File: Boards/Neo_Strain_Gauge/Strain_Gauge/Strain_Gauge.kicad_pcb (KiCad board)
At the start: 2 copper layers, 85 x 56 mm, 60 parts, among them J1 Screw_Terminal_01x03, J2 Screw_Terminal_01x03, J3 Screw_Terminal_01x03, J4 Screw_Terminal_01x03, J5 Conn_01x02, J6 USB_B_Micro, J7 Conn_02x10_Counter_Clockwise, J8 Conn_02x12_Counter_Clockwise, U1 W25Q128JVS, U2 NCP1117-3.3_SOT223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

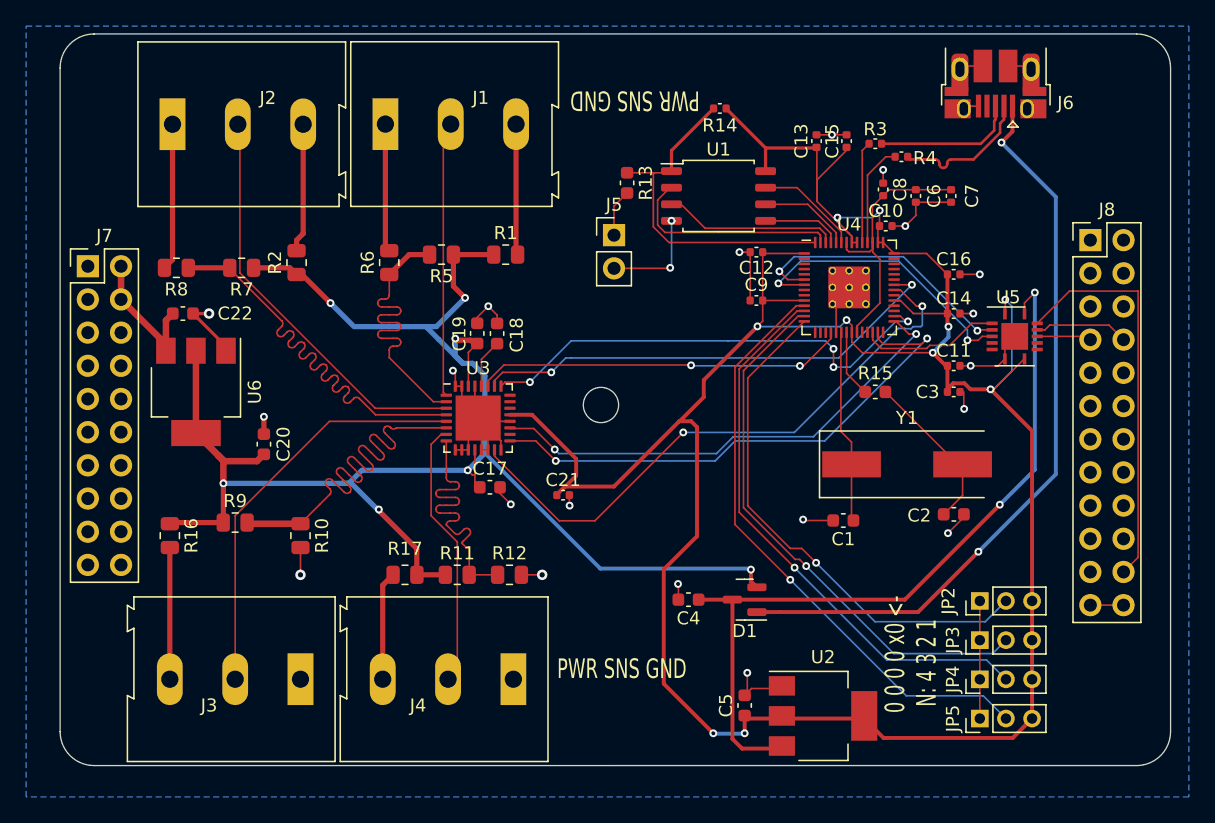
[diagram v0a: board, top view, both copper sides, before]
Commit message: Remove a LOT of signal noise on the oscillator
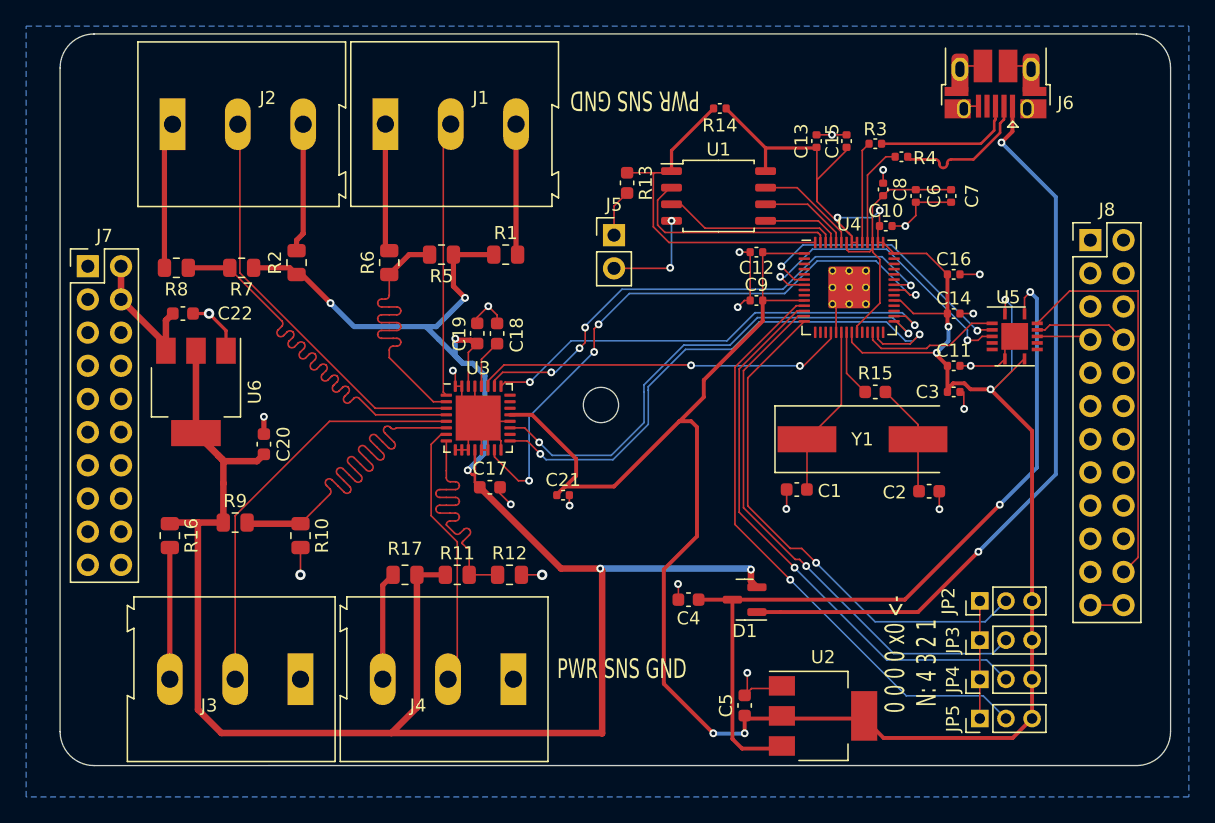
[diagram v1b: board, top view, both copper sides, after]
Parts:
- moved C1 4.28 mm to (157.0, 88.5)
- moved Y1 3.91 mm to (162.0, 84.6)
- moved C2 2.59 mm to (167.1, 88.6)
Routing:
- net +5V: track 132.9 -> 174.9 mm, vias 7 -> 6
- net +3V3: track 208.4 -> 200.2 mm, vias 10 -> 8
- net Net-(C2-Pad1): track 12.6 -> 8.66 mm
- net /GPIO24: track 36.8 -> 39.2 mm, vias 2 -> 4
- net /GPIO16: track 41.0 -> 43.0 mm
- net /XIN: track 14.8 -> 13.1 mm
- net /GPIO23: track 45.6 -> 47.3 mm, vias 2 -> 4
- net /GPIO18: track 37.8 -> 39.4 mm
- net GND: track 116.8 -> 116.1 mm, vias 22 -> 23
- net /GPIO19: track 36.7 -> 36.3 mm, vias 4 -> 2

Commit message: Anti-emi Aktion
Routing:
- net +5V: track 174.9 -> 226.2 mm, vias 6 -> 5
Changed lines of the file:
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@@
   (target plus (at 180.5 104.1) (size 5) (width 0.1) (layer "Edge.Cuts"))
   (segment (start 132.35 87.925) (end 132.725 88.3) (width 0.2) (layer "F.Cu") (net 1))
-  (segment (start 130.7075 70.49) (end 133.795 70.49) (width 0.4) (layer "F.Cu") (net 1))
   (segment (start 132.035 77.04) (end 130.97 77.04) (width 0.4) (layer "F.Cu") (net 1))
   (segment (start 130.0875 95) (end 127.9125 95) (width 0.4) (layer "F.Cu") (net 1))
@@
   (segment (start 111.15 91) (end 109.0875 91) (width 0.5) (layer "F.Cu") (net 1))
   (segment (start 132.29 77.295) (end 132.53 77.295) (width 0.4) (layer "F.Cu") (net 1))
-  (segment (start 131.6 73.8) (end 130.7075 72.9075) (width 0.4) (layer "F.Cu") (net 1))
+  (segment (start 121.59 69.57) (end 121.555 69.57) (width 0.5) (layer "F.Cu") (net 1))
   (segment (start 109.0875 91) (end 109 91.0875) (width 0.5) (layer "F.Cu") (net 1))
   (segment (start 115.4125 71.5) (end 118.1875 71.5) (width 0.4) (layer "F.Cu") (net 1))
   (segment (start 138.945 94.52) (end 132.725 88.3) (width 0.5) (layer "F.Cu") (net 1))
-  (segment (start 131.8 87) (end 132.15 87.35) (width 0.2) (layer "F.Cu") (net 1))
   (segment (start 111.15 105.31) (end 112.95 107.11) (width 0.5) (layer "F.Cu") (net 1))
   (segment (start 113.1 88) (end 113.1 90.9875) (width 0.5) (layer "F.Cu") (net 1))
   (segment (start 111.15 91) (end 111.15 105.31) (width 0.5) (layer "F.Cu") (net 1))
-  (segment (start 132.15 87.35) (end 132.35 87.35) (width 0.2) (layer "F.Cu") (net 1))
-  (segment (start 130.7075 72.9075) (end 130.7075 70.49) (width 0.4) (layer "F.Cu") (net 1))
+  (segment (start 130.7075 76.7875) (end 130.7075 70.49) (width 0.4) (layer "F.Cu") (net 1))
   (segment (start 141.947 94.52) (end 138.945 94.52) (width 0.5) (layer "F.Cu") (net 1))
   (segment (start 127.9125 105.1575) (end 127.9125 95) (width 0.5) (layer "F.Cu") (net 1))
   (segment (start 113.1 86.25) (end 113 86.15) (width 0.5) (layer "F.Cu") (net 1))
   (segment (start 131.85 80.5625) (end 131.85 77.975) (width 0.127) (layer "F.Cu") (net 1))
+  (segment (start 132.53 70.49) (end 133.795 70.49) (width 0.4) (layer "F.Cu") (net 1))
+  (segment (start 130.97 77.04) (end 130.96 77.04) (width 0.4) (layer "F.Cu") (net 1))
   (segment (start 142.09 107.14) (end 142.09 94.663) (width 0.5) (layer "F.Cu") (net 1))
   (segment (start 112.7 85.85) (end 113.15 86.3) (width 0.5) (layer "F.Cu") (net 1))
@@
   (segment (start 113.1 88) (end 113.1 86.25) (width 0.5) (layer "F.Cu") (net 1))
   (segment (start 113.1 90.9875) (end 113.0875 91) (width 0.5) (layer "F.Cu") (net 1))
+  (segment (start 130.7075 70.49) (end 132.53 70.49) (width 0.4) (layer "F.Cu") (net 1))
   (segment (start 125.96 107.11) (end 142.06 107.11) (width 0.5) (layer "F.Cu") (net 1))
   (segment (start 132.35 87.35) (end 132.35 87.925) (width 0.2) (layer "F.Cu") (net 1))
-  (segment (start 118.7 72.0125) (end 119.1125 72.0125) (width 0.127) (layer "F.Cu") (net 1))
   (segment (start 111 84.15) (end 111 77.85) (width 0.5) (layer "F.Cu") (net 1))
   (segment (start 153.48 95.4925) (end 153.9375 95.95) (width 0.5) (layer "F.Cu") (net 1))
   (segment (start 153.48 94.6) (end 153.48 95.4925) (width 0.5) (layer "F.Cu") (net 1))
   (segment (start 132.35 85.4375) (end 132.35 87.35) (width 0.2) (layer "F.Cu") (net 1))
+  (segment (start 111 77.85) (end 111 77.22) (width 0.5) (layer "F.Cu") (net 1))
   (segment (start 132.035 77.04) (end 132.29 77.295) (width 0.4) (layer "F.Cu") (net 1))
   (segment (start 131.85 77.975) (end 132.53 77.295) (width 0.127) (layer "F.Cu") (net 1))
@@
   (segment (start 112.7 85.85) (end 113 86.15) (width 0.5) (layer "F.Cu") (net 1))
   (segment (start 112.95 107.11) (end 125.96 107.11) (width 0.5) (layer "F.Cu") (net 1))
-  (segment (start 119.1125 72.0125) (end 121.3 74.2) (width 0.4) (layer "F.Cu") (net 1))
+  (segment (start 121.555 69.57) (end 119.1125 72.0125) (width 0.5) (layer "F.Cu") (net 1))
   (segment (start 142.06 107.11) (end 142.09 107.14) (width 0.5) (layer "F.Cu") (net 1))
+  (segment (start 130.96 77.04) (end 130.7075 76.7875) (width 0.4) (layer "F.Cu") (net 1))
   (segment (start 130.97 77.04) (end 130.85 76.92) (width 0.4) (layer "F.Cu") (net 1))
+  (segment (start 119.1125 72.0125) (end 118.7 72.0125) (width 0.5) (layer "F.Cu") (net 1))
+  (segment (start 111 77.22) (end 109.94 76.16) (width 0.5) (layer "F.Cu") (net 1))
   (segment (start 142.09 94.663) (end 141.947 94.52) (width 0.5) (layer "F.Cu") (net 1))
   (segment (start 125.96 107.11) (end 127.9125 105.1575) (width 0.5) (layer "F.Cu") (net 1))
-  (via (at 131.6 73.8) (size 0.6) (drill 0.3) (layers "F.Cu" "B.Cu") (net 1))
+  (via (at 132.53 70.49) (size 0.6) (drill 0.3) (layers "F.Cu" "B.Cu") (net 1))
   (via (at 153.48 94.6) (size 0.6) (drill 0.3) (layers "F.Cu" "B.Cu") (net 1))
-  (via (at 121.3 74.2) (size 0.6) (drill 0.3) (layers "F.Cu" "B.Cu") (net 1))
+  (via (at 121.59 69.57) (size 0.6) (drill 0.3) (layers "F.Cu" "B.Cu") (net 1))
   (via (at 141.947 94.52) (size 0.6) (drill 0.3) (layers "F.Cu" "B.Cu") (net 1))
-  (via (at 131.8 87) (size 0.6) (drill 0.3) (layers "F.Cu" "B.Cu") (net 1))
-  (via (at 130.85 76.92) (size 0.6) (drill 0.3) (layers "F.Cu" "B.Cu") (net 1))
-  (segment (start 132.17 78.81) (end 131.41 78.81) (width 0.4) (layer "B.Cu") (net 1))
-  (segment (start 133.1135 79.7535) (end 133.1135 85.6865) (width 0.4) (layer "B.Cu") (net 1))
+  (via (at 109.94 76.16) (size 0.6) (drill 0.3) (layers "F.Cu" "B.Cu") (net 1))
+  (segment (start 132.53 57.64) (end 132.53 70.49) (width 0.5) (layer "B.Cu") (net 1))
   (segment (start 153.4 94.52) (end 141.947 94.52) (width 0.5) (layer "B.Cu") (net 1))
-  (segment (start 129.575 76.975) (end 128.6 76) (width 0.4) (layer "B.Cu") (net 1))
-  (segment (start 128.6 76) (end 129.4 76) (width 0.4) (layer "B.Cu") (net 1))
-  (segment (start 130.85 78.25) (end 131.41 78.81) (width 0.4) (layer "B.Cu") (net 1))
-  (segment (start 128.6 76) (end 125.2 76) (width 0.4) (layer "B.Cu") (net 1))
-  (segment (start 130.85 76.92) (end 130.85 78.25) (width 0.4) (layer "B.Cu") (net 1))
+  (segment (start 121.59 69.57) (end 122.68 68.48) (width 0.5) (layer "B.Cu") (net 1))
+  (segment (start 107.32 55.99) (end 121.67 55.99) (width 0.5) (layer "B.Cu") (net 1))
+  (segment (start 107.32 72.22) (end 107.32 55.99) (width 0.5) (layer "B.Cu") (net 1))
   (segment (start 153.48 94.6) (end 153.4 94.52) (width 0.5) (layer "B.Cu") (net 1))
-  (segment (start 125.2 76) (end 123.1 76) (width 0.4) (layer "B.Cu") (net 1))
-  (segment (start 132.17 78.81) (end 133.1135 79.7535) (width 0.4) (layer "B.Cu") (net 1))
-  (segment (start 129.4 76) (end 131.6 73.8) (width 0.4) (layer "B.Cu") (net 1))
-  (segment (start 131.41 78.81) (end 129.575 76.975) (width 0.4) (layer "B.Cu") (net 1))
-  (segment (start 123.1 76) (end 123 75.9) (width 0.127) (layer "B.Cu") (net 1))
-  (segment (start 123 75.9) (end 121.3 74.2) (width 0.4) (layer "B.Cu") (net 1))
-  (segment (start 133.1135 85.6865) (end 131.8 87) (width 0.4) (layer "B.Cu") (net 1))
+  (segment (start 130.88 55.99) (end 132.53 57.64) (width 0.5) (layer "B.Cu") (net 1))
+  (segment (start 109.94 74.84) (end 107.32 72.22) (width 0.5) (layer "B.Cu") (net 1))
+  (segment (start 122.68 68.48) (end 122.68 57) (width 0.5) (layer "B.Cu") (net 1))
+  (segment (start 122.68 57) (end 121.67 55.99) (width 0.5) (layer "B.Cu") (net 1))
+  (segment (start 109.94 76.16) (end 109.94 74.84) (width 0.5) (layer "B.Cu") (net 1))
+  (segment (start 121.67 55.99) (end 130.88 55.99) (width 0.5) (layer "B.Cu") (net 1))
   (segment (start 170.3 79) (end 169.48 79) (width 0.127) (layer "F.Cu") (net 2))
   (segment (start 169.725 56.05) (end 169.475 56.3) (width 0.127) (layer "F.Cu") (net 2))
@@
   (segment (start 182 77) (end 180.8865 75.8865) (width 0.127) (layer "F.Cu") (net 41))
   (segment (start 176.3505 75.8865) (end 175.987 76.25) (width 0.127) (layer "F.Cu") (net 41))
-  (segment (start 183.13 73.28) (end 177.865 73.28) (width 0.127) (layer "F.Cu") (net 52))
   (segment (start 177.865 73.28) (end 175.395 75.75) (width 0.127) (layer "F.Cu") (net 52))
-  (segment (start 183.1135 93.6665) (end 183.1135 73.2965) (width 0.127) (layer "F.Cu") (net 52))
-  (segment (start 183.1135 73.2965) (end 183.13 73.28) (width 0.127) (layer "F.Cu") (net 52))
-  (segment (start 182 94.78) (end 183.1135 93.6665) (width 0.127) (layer "F.Cu") (net 52))
+  (segment (start 182 94.78) (end 183.35 93.43) (width 0.127) (layer "F.Cu") (net 52))
+  (segment (start 182.57 73.28) (end 177.865 73.28) (width 0.127) (layer "F.Cu") (net 52))
+  (segment (start 183.35 74.06) (end 182.57 73.28) (width 0.127) (layer "F.Cu") (net 52))
+  (segment (start 183.35 93.43) (end 183.35 74.06) (width 0.127) (layer "F.Cu") (net 52))
   (segment (start 179.46 97.32) (end 182 97.32) (width 0.127) (layer "F.Cu") (net 53))
   (segment (start 157.5625 74.4) (end 156.956748 74.4) (width 0.127) (layer "F.Cu") (net 54))

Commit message: Micro-optimized it all.
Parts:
- moved C21 3.98 mm to (138.4, 85.0), turned to -90 degrees
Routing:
- net +3V3: track 200.2 -> 193.4 mm
- net +5V: track 226.2 -> 224.5 mm
- net GND: track 116.1 -> 117.3 mm
- net /VBUS: track 57.5 -> 56.8 mm

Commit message: PCB update before I decide to go off and do wild changes
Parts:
- moved C3 1.02 mm to (169.0, 80.0)
- moved R2 0.49 mm to (118.7, 70.6)
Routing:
- net +3V3: track 193.4 -> 192.2 mm
- net GND: track 117.3 -> 117.0 mm, vias 23 -> 22

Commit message: Begin working on the pico driver
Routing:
- net GND: track 117.0 -> 110.0 mm, vias 22 -> 21
- net /QSPI_SD1: track 16.7 -> 17.4 mm
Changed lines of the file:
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@@
   (segment (start 134.3365 85.424) (end 134.3365 84.7365) (width 0.127) (layer "F.Cu") (net 2))
   (segment (start 108.5875 61.1275) (end 108.5875 71.5) (width 0.4) (layer "F.Cu") (net 2))
+  (segment (start 147.515 67.905) (end 147.4 67.905) (width 0.127) (layer "F.Cu") (net 2))
   (segment (start 133.35 83.75) (end 132.6 83) (width 0.127) (layer "F.Cu") (net 2))
   (segment (start 152.47 74.51) (end 152.98 74) (width 0.127) (layer "F.Cu") (net 2))
@@
   (segment (start 172.92 77.5) (end 172.92 78.475) (width 0.127) (layer "F.Cu") (net 2))
   (segment (start 164.28 68.3) (end 165.3 68.3) (width 0.127) (layer "F.Cu") (net 2))
-  (segment (start 143 71.54) (end 147.26 71.54) (width 0.127) (layer "F.Cu") (net 2))
   (segment (start 147.925 96.9) (end 147.925 95.725) (width 0.127) (layer "F.Cu") (net 2))
   (segment (start 138.41 87.47) (end 138.41 85.48) (width 0.127) (layer "F.Cu") (net 2))
@@
   (segment (start 166.1 66.48) (end 166.1 67.5) (width 0.127) (layer "F.Cu") (net 2))
   (segment (start 160.8 61.32) (end 159.68 61.32) (width 0.127) (layer "F.Cu") (net 2))
-  (segment (start 147.26 71.54) (end 147.3 71.5) (width 0.127) (layer "F.Cu") (net 2))
   (segment (start 132.85 83.25) (end 132.6 83) (width 0.127) (layer "F.Cu") (net 2))
   (segment (start 171 106) (end 171 103) (width 0.127) (layer "F.Cu") (net 2))
   (segment (start 153.42 74) (end 153.42 70.3) (width 0.127) (layer "F.Cu") (net 2))
+  (segment (start 148.13 68.52) (end 147.515 67.905) (width 0.127) (layer "F.Cu") (net 2))
   (segment (start 132.35 80.5625) (end 132.35 82.75) (width 0.127) (layer "F.Cu") (net 2))
   (via (at 152.6 70.3) (size 0.6) (drill 0.3) (layers "F.Cu" "B.Cu") (net 2))
@@
   (via (at 130.67 79.37) (size 0.6) (drill 0.3) (layers "F.Cu" "B.Cu") (net 2))
   (via (at 137.5 95) (size 0.8) (drill 0.4) (layers "F.Cu" "B.Cu") (net 2))
+  (via (at 148.13 68.52) (size 0.6) (drill 0.3) (layers "F.Cu" "B.Cu") (net 2))
   (via (at 138.41 87.47) (size 0.6) (drill 0.3) (layers "F.Cu" "B.Cu") (net 2))
   (via (at 153.2 102.5) (size 0.6) (drill 0.3) (layers "F.Cu" "B.Cu") (net 2))
@@
   (via (at 135.1 89.6) (size 0.6) (drill 0.3) (layers "F.Cu" "B.Cu") (net 2))
   (via (at 156.19 89.96) (size 0.6) (drill 0.3) (layers "F.Cu" "B.Cu") (net 2))
-  (via (at 147.3 71.5) (size 0.6) (drill 0.3) (layers "F.Cu" "B.Cu") (net 2))
   (via (at 170.5 75) (size 0.6) (drill 0.3) (layers "F.Cu" "B.Cu") (net 2))
   (via (at 152.47 74.51) (size 0.6) (drill 0.3) (layers "F.Cu" "B.Cu") (net 2))
   (via (at 165.3 68.3) (size 0.6) (drill 0.3) (layers "F.Cu" "B.Cu") (net 2))
   (via (at 116.2 82.9) (size 0.6) (drill 0.3) (layers "F.Cu" "B.Cu") (net 2))
-  (via (at 147.4 67.9) (size 0.6) (drill 0.3) (layers "F.Cu" "B.Cu") (net 2))
   (via (at 163.6 64) (size 0.6) (drill 0.3) (layers "F.Cu" "B.Cu") (net 2))
   (via (at 167.91 89.98) (size 0.6) (drill 0.3) (layers "F.Cu" "B.Cu") (net 2))
   (via (at 147.9 95.7) (size 0.6) (drill 0.3) (layers "F.Cu" "B.Cu") (net 2))
-  (segment (start 147.4 71.4) (end 147.4 67.9) (width 0.127) (layer "B.Cu") (net 2))
-  (segment (start 147.3 71.5) (end 147.4 71.4) (width 0.127) (layer "B.Cu") (net 2))
   (segment (start 157.77 84.62) (end 160.4 81.99) (width 0.127) (layer "F.Cu") (net 3))
   (segment (start 157.77 88.465) (end 157.77 84.62) (width 0.127) (layer "F.Cu") (net 3))
@@
   (segment (start 144 64.225) (end 146.1 64.225) (width 0.127) (layer "F.Cu") (net 62))
   (segment (start 147.4 62.52) (end 150.62 59.3) (width 0.25) (layer "F.Cu") (net 62))
-  (segment (start 147.210275 69.5625) (end 158.4 69.5625) (width 0.127) (layer "F.Cu") (net 62))
+  (segment (start 146.5625 69.5625) (end 158.4 69.5625) (width 0.127) (layer "F.Cu") (net 62))
+  (segment (start 146.0095 69.0095) (end 146.5625 69.5625) (width 0.127) (layer "F.Cu") (net 62))
   (segment (start 146.1 64.225) (end 147.27 64.225) (width 0.127) (layer "F.Cu") (net 62))
-  (segment (start 146.0095 64.3155) (end 146.1 64.225) (width 0.127) (layer "F.Cu") (net 62))
-  (segment (start 146.0095 64.3155) (end 146.0095 68.361725) (width 0.127) (layer "F.Cu") (net 62))
+  (segment (start 146.1 64.225) (end 146.0095 64.3155) (width 0.127) (layer "F.Cu") (net 62))
   (segment (start 147.27 64.225) (end 147.4 64.095) (width 0.25) (layer "F.Cu") (net 62))
-  (segment (start 146.0095 68.361725) (end 147.210275 69.5625) (width 0.127) (layer "F.Cu") (net 62))
   (segment (start 147.4 64.095) (end 147.4 62.52) (width 0.25) (layer "F.Cu") (net 62))
+  (segment (start 146.0095 64.3155) (end 146.0095 69.0095) (width 0.127) (layer "F.Cu") (net 62))
   (segment (start 160.8 76.4375) (end 160.8 79.575) (width 0.127) (layer "F.Cu") (net 63))
   (segment (start 160.8 79.575) (end 162.225 81) (width 0.127) (layer "F.Cu") (net 63))
-  (segment (start 158.8 69) (end 158.5955 68.7955) (width 0.127) (layer "F.Cu") (net 64))
-  (segment (start 158.5955 68.7955) (end 146.905723 68.7955) (width 0.127) (layer "F.Cu") (net 64))
-  (segment (start 146.3365 68.226277) (end 146.3365 66.313723) (width 0.127) (layer "F.Cu") (net 64))
-  (segment (start 146.905723 68.7955) (end 146.3365 68.226277) (width 0.127) (layer "F.Cu") (net 64))
+  (segment (start 146.3365 66.313723) (end 147.285223 65.365) (width 0.127) (layer "F.Cu") (net 64))
+  (segment (start 158.220144 68.8615) (end 157.846144 69.2355) (width 0.127) (layer "F.Cu") (net 64))
+  (segment (start 146.3365 68.874052) (end 146.3365 66.313723) (width 0.127) (layer "F.Cu") (net 64))
+  (segment (start 158.8 69) (end 158.6615 68.8615) (width 0.127) (layer "F.Cu") (net 64))
+  (segment (start 157.846144 69.2355) (end 146.697948 69.2355) (width 0.127) (layer "F.Cu") (net 64))
+  (segment (start 158.6615 68.8615) (end 158.220144 68.8615) (width 0.127) (layer "F.Cu") (net 64))
+  (segment (start 158.8 69.5625) (end 158.8 69) (width 0.127) (layer "F.Cu") (net 64))
+  (segment (start 146.697948 69.2355) (end 146.3365 68.874052) (width 0.127) (layer "F.Cu") (net 64))
   (segment (start 147.285223 65.365) (end 147.4 65.365) (width 0.127) (layer "F.Cu") (net 64))
-  (segment (start 146.3365 66.313723) (end 147.285223 65.365) (width 0.127) (layer "F.Cu") (net 64))
-  (segment (start 158.8 69.5625) (end 158.8 69) (width 0.127) (layer "F.Cu") (net 64))
   (segment (start 148.135 66.635) (end 147.4 66.635) (width 0.127) (layer "F.Cu") (net 65))
   (segment (start 159.2 69.5625) (end 159.2 68.931436) (width 0.127) (layer "F.Cu") (net 65))
